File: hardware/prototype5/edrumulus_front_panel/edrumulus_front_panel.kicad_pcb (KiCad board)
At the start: 2 copper layers, 65 x 56.5 mm, 22 parts, among them J2 Raspberry Pi GPIO pins, SW1 SW_Push, SW2 SW_Push, SW3 SW_Push, SW4 SW_Push, SW5 SW_Push, SW6 SW_Push

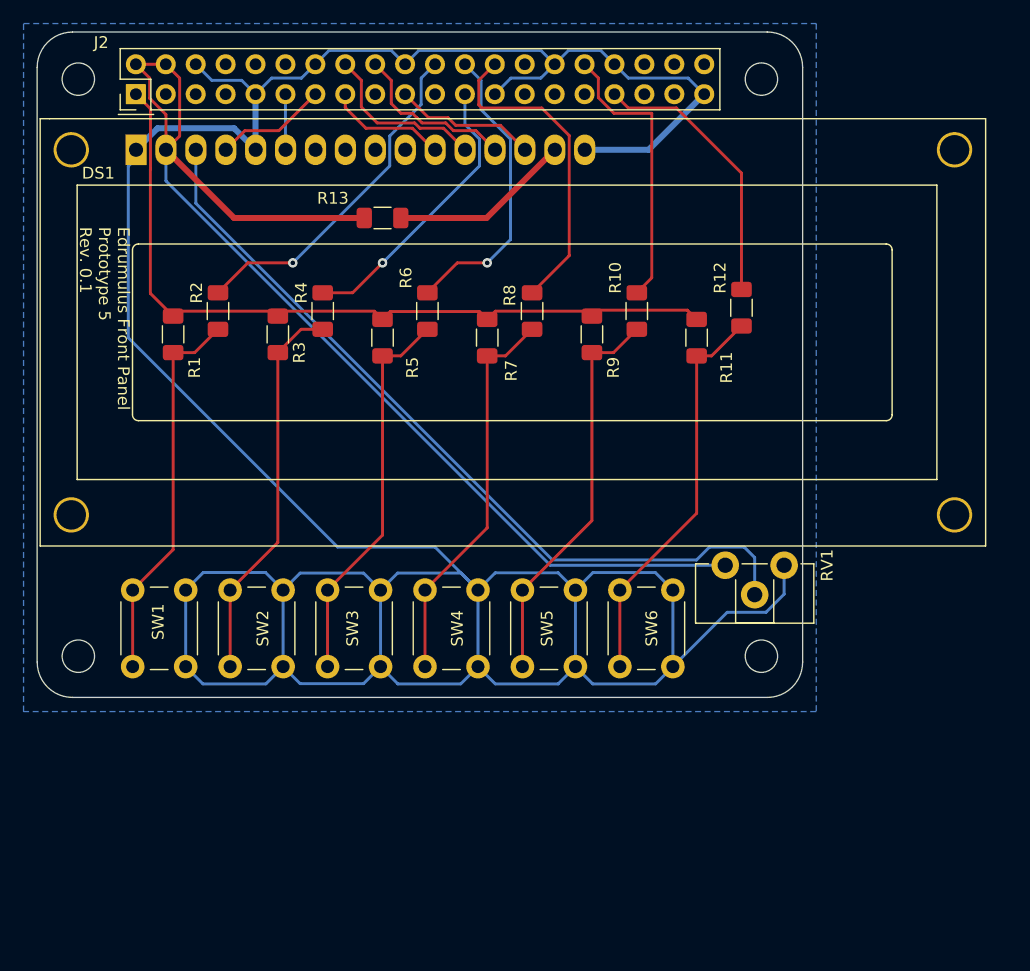
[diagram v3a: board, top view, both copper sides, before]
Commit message: fixes for the front panel for prototype 5
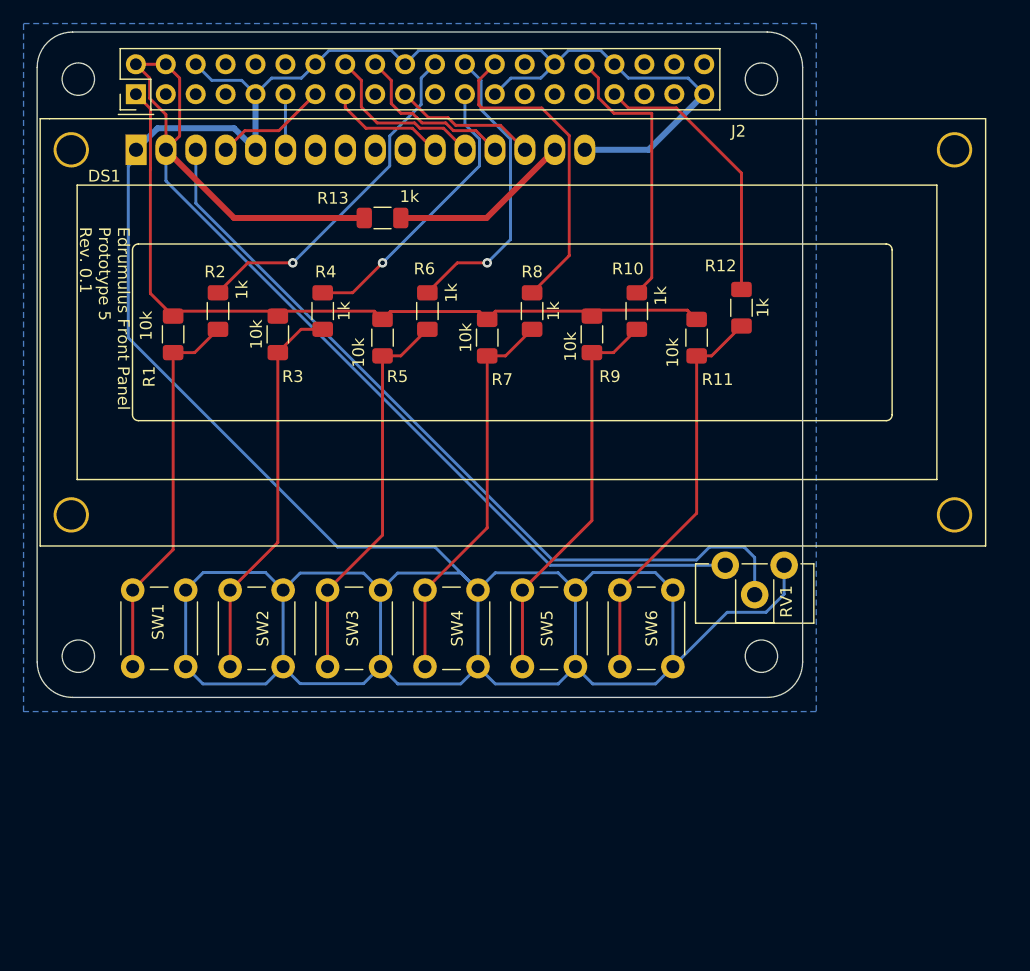
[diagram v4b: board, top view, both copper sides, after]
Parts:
- R13: value 470 -> 1k
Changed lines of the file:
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@@
   (net 4 "unconnected-(DS1-Pad7)")
   (net 5 "5V")
-  (net 6 "Net-(RV1-Pad2)")
+  (net 6 "Net-(DS1-Pad3)")
   (net 7 "PI-GPIO27")
   (net 8 "PI-GPIO17")
@@
     (property "Sheetname" "")
     (attr through_hole)
-    (fp_text reference "J2" (at 4.386211 -2.94664 180) (layer "F.SilkS")
+    (fp_text reference "J2" (at -3.147789 51.16936 180) (layer "F.SilkS")
       (effects (font (size 1 1) (thickness 0.15)))
     )
@@
     (property "Sheetname" "")
     (attr smd)
-    (fp_text reference "R8" (at 1.333014 -1.891939 90) (layer "F.SilkS")
-      (effects (font (size 1 1) (thickness 0.15)))
-    )
-    (fp_text value "1k" (at 0 1.82 90) (layer "F.Fab")
+    (fp_text reference "R8" (at 3.328 0 180) (layer "F.SilkS")
+      (effects (font (size 1 1) (thickness 0.15)))
+    )
+    (fp_text value "1k" (at 0 1.82 90) (layer "F.SilkS")
       (effects (font (size 1 1) (thickness 0.15)))
     )
@@
     (property "Sheetname" "")
     (attr smd)
-    (fp_text reference "R5" (at 2.54 -2.54 90) (layer "F.SilkS")
-      (effects (font (size 1 1) (thickness 0.15)))
-    )
-    (fp_text value "10k" (at 0 1.82 90) (layer "F.Fab")
+    (fp_text reference "R5" (at 3.302 -1.27 180) (layer "F.SilkS")
+      (effects (font (size 1 1) (thickness 0.15)))
+    )
+    (fp_text value "10k" (at 1.27 2.032 90) (layer "F.SilkS")
       (effects (font (size 1 1) (thickness 0.15)))
     )
@@
     (property "Sheetname" "")
     (attr smd)
-    (fp_text reference "R9" (at 2.82 -1.82 90) (layer "F.SilkS")
-      (effects (font (size 1 1) (thickness 0.15)))
-    )
-    (fp_text value "10k" (at 0 1.82 90) (layer "F.Fab")
+    (fp_text reference "R9" (at 3.582 -1.524 180) (layer "F.SilkS")
+      (effects (font (size 1 1) (thickness 0.15)))
+    )
+    (fp_text value "10k" (at 1.042 1.82 90) (layer "F.SilkS")
       (effects (font (size 1 1) (thickness 0.15)))
     )
@@
     (property "Sheetname" "")
     (attr smd)
-    (fp_text reference "R1" (at 2.82 -1.82 90) (layer "F.SilkS")
-      (effects (font (size 1 1) (thickness 0.15)))
-    )
-    (fp_text value "10k" (at 0 1.82 90) (layer "F.Fab")
+    (fp_text reference "R1" (at 3.582 2.032 90) (layer "F.SilkS")
+      (effects (font (size 1 1) (thickness 0.15)))
+    )
+    (fp_text value "10k" (at -0.736 2.286 90) (layer "F.SilkS")
       (effects (font (size 1 1) (thickness 0.15)))
     )
@@
     (property "Sheetname" "")
     (attr smd)
-    (fp_text reference "R11" (at 2.54 -2.54 90) (layer "F.SilkS")
-      (effects (font (size 1 1) (thickness 0.15)))
-    )
-    (fp_text value "10k" (at 0 1.82 90) (layer "F.Fab")
+    (fp_text reference "R11" (at 3.556 -1.778 180) (layer "F.SilkS")
+      (effects (font (size 1 1) (thickness 0.15)))
+    )
+    (fp_text value "10k" (at 1.27 2.032 90) (layer "F.SilkS")
       (effects (font (size 1 1) (thickness 0.15)))
     )
@@
     (property "Sheetname" "")
     (attr smd)
-    (fp_text reference "R7" (at 2.80126 -2.037804 90) (layer "F.SilkS")
-      (effects (font (size 1 1) (thickness 0.15)))
-    )
-    (fp_text value "10k" (at 0 1.82 90) (layer "F.Fab")
+    (fp_text reference "R7" (at 3.556 -1.27 180) (layer "F.SilkS")
+      (effects (font (size 1 1) (thickness 0.15)))
+    )
+    (fp_text value "10k" (at 0 1.82 90) (layer "F.SilkS")
       (effects (font (size 1 1) (thickness 0.15)))
     )
@@
     (property "Sheetname" "")
     (attr smd)
-    (fp_text reference "R10" (at 2.82 -1.82 90) (layer "F.SilkS")
-      (effects (font (size 1 1) (thickness 0.15)))
-    )
-    (fp_text value "1k" (at 0 1.82 90) (layer "F.Fab")
+    (fp_text reference "R10" (at 3.582 -0.762 180) (layer "F.SilkS")
+      (effects (font (size 1 1) (thickness 0.15)))
+    )
+    (fp_text value "1k" (at 1.296 2.032 90) (layer "F.SilkS")
       (effects (font (size 1 1) (thickness 0.15)))
     )
@@
     (property "Sheetname" "")
     (attr smd)
-    (fp_text reference "R4" (at 1.55 -1.82 90) (layer "F.SilkS")
-      (effects (font (size 1 1) (thickness 0.15)))
-    )
-    (fp_text value "1k" (at 0 1.82 90) (layer "F.Fab")
+    (fp_text reference "R4" (at 3.328 0.254 180) (layer "F.SilkS")
+      (effects (font (size 1 1) (thickness 0.15)))
+    )
+    (fp_text value "1k" (at 0 1.82 90) (layer "F.SilkS")
       (effects (font (size 1 1) (thickness 0.15)))
     )
@@
     (property "Sheetname" "")
     (attr through_hole)
-    (fp_text reference "RV1" (at 0 -3.65 -90) (layer "F.SilkS")
+    (fp_text reference "RV1" (at 3.077208 -0.192191 -90) (layer "F.SilkS")
       (effects (font (size 1 1) (thickness 0.15)))
     )
@@
       (net 1 "GND") (pinfunction "1") (pintype "passive"))
     (pad "2" thru_hole circle (at 2.5 2.5 270) (size 2.34 2.34) (drill 1.3) (layers *.Cu *.Mask)
-      (net 6 "Net-(RV1-Pad2)") (pinfunction "2") (pintype "passive"))
+      (net 6 "Net-(DS1-Pad3)") (pinfunction "2") (pintype "passive"))
     (pad "3" thru_hole circle (at 0 5 270) (size 2.34 2.34) (drill 1.3) (layers *.Cu *.Mask)
       (net 5 "5V") (pinfunction "3") (pintype "passive"))
@@
       (effects (font (size 1 1) (thickness 0.15)))
     )
-    (fp_text value "470" (at 0 1.82) (layer "F.Fab")
+    (fp_text value "1k" (at -2.286 1.82) (layer "F.SilkS")
       (effects (font (size 1 1) (thickness 0.15)))
     )
@@
     (property "Sheetname" "")
     (attr smd)
-    (fp_text reference "R3" (at 1.55 -1.82 90) (layer "F.SilkS")
-      (effects (font (size 1 1) (thickness 0.15)))
-    )
-    (fp_text value "10k" (at 0 1.82 90) (layer "F.Fab")
+    (fp_text reference "R3" (at 3.582 -1.27 180) (layer "F.SilkS")
+      (effects (font (size 1 1) (thickness 0.15)))
+    )
+    (fp_text value "10k" (at 0 1.82 90) (layer "F.SilkS")
       (effects (font (size 1 1) (thickness 0.15)))
     )
@@
     (property "Sheetname" "")
     (attr smd)
-    (fp_text reference "R6" (at 2.82 -1.82 90) (layer "F.SilkS")
-      (effects (font (size 1 1) (thickness 0.15)))
-    )
-    (fp_text value "1k" (at 0 1.82 90) (layer "F.Fab")
+    (fp_text reference "R6" (at 3.582 -0.254 180) (layer "F.SilkS")
+      (effects (font (size 1 1) (thickness 0.15)))
+    )
+    (fp_text value "1k" (at 1.55 2.032 90) (layer "F.SilkS")
       (effects (font (size 1 1) (thickness 0.15)))
     )
@@
     (property "Sheetname" "")
     (attr smd)
-    (fp_text reference "R2" (at 1.55 -1.82 90) (layer "F.SilkS")
-      (effects (font (size 1 1) (thickness 0.15)))
-    )
-    (fp_text value "1k" (at 0 1.82 90) (layer "F.Fab")
+    (fp_text reference "R2" (at 3.328 -0.254 180) (layer "F.SilkS")
+      (effects (font (size 1 1) (thickness 0.15)))
+    )
+    (fp_text value "1k" (at 1.804 2.032 90) (layer "F.SilkS")
       (effects (font (size 1 1) (thickness 0.15)))
     )
@@
     (property "Sheetname" "")
     (attr through_hole)
-    (fp_text reference "DS1" (at -3.2004 1.9812) (layer "F.SilkS")
+    (fp_text reference "DS1" (at -2.6924 2.2352) (layer "F.SilkS")
       (effects (font (size 1 1) (thickness 0.15)))
     )
@@
       (net 5 "5V") (pinfunction "VDD") (pintype "power_in"))
     (pad "3" thru_hole oval (at 5.08 0) (size 1.8 2.6) (drill 1.2) (layers *.Cu *.Mask)
-      (net 6 "Net-(RV1-Pad2)") (pinfunction "VO") (pintype "input"))
+      (net 6 "Net-(DS1-Pad3)") (pinfunction "VO") (pintype "input"))
     (pad "4" thru_hole oval (at 7.62 0) (size 1.8 2.6) (drill 1.2) (layers *.Cu *.Mask)
       (net 7 "PI-GPIO27") (pinfunction "RS") (pintype "input"))
@@
     (property "Sheetname" "")
     (attr smd)
-    (fp_text reference "R12" (at 2.54 -1.82 90) (layer "F.SilkS")
-      (effects (font (size 1 1) (thickness 0.15)))
-    )
-    (fp_text value "1k" (at 0 1.82 90) (layer "F.Fab")
-      (effects (font (size 1 1) (thickness 0.15)))
-    )
+    (fp_text reference "R12" (at 3.556 -1.778 180) (layer "F.SilkS")
+      (effects (font (size 1 1) (thickness 0.15)))
+    )
+    (fp_text value "1k" (at 0 1.82 90) (layer "F.SilkS")
+      (effects (font (size 1 1) (thickness 0.15)))
+    )
